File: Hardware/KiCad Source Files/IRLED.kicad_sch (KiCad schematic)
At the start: 14 parts

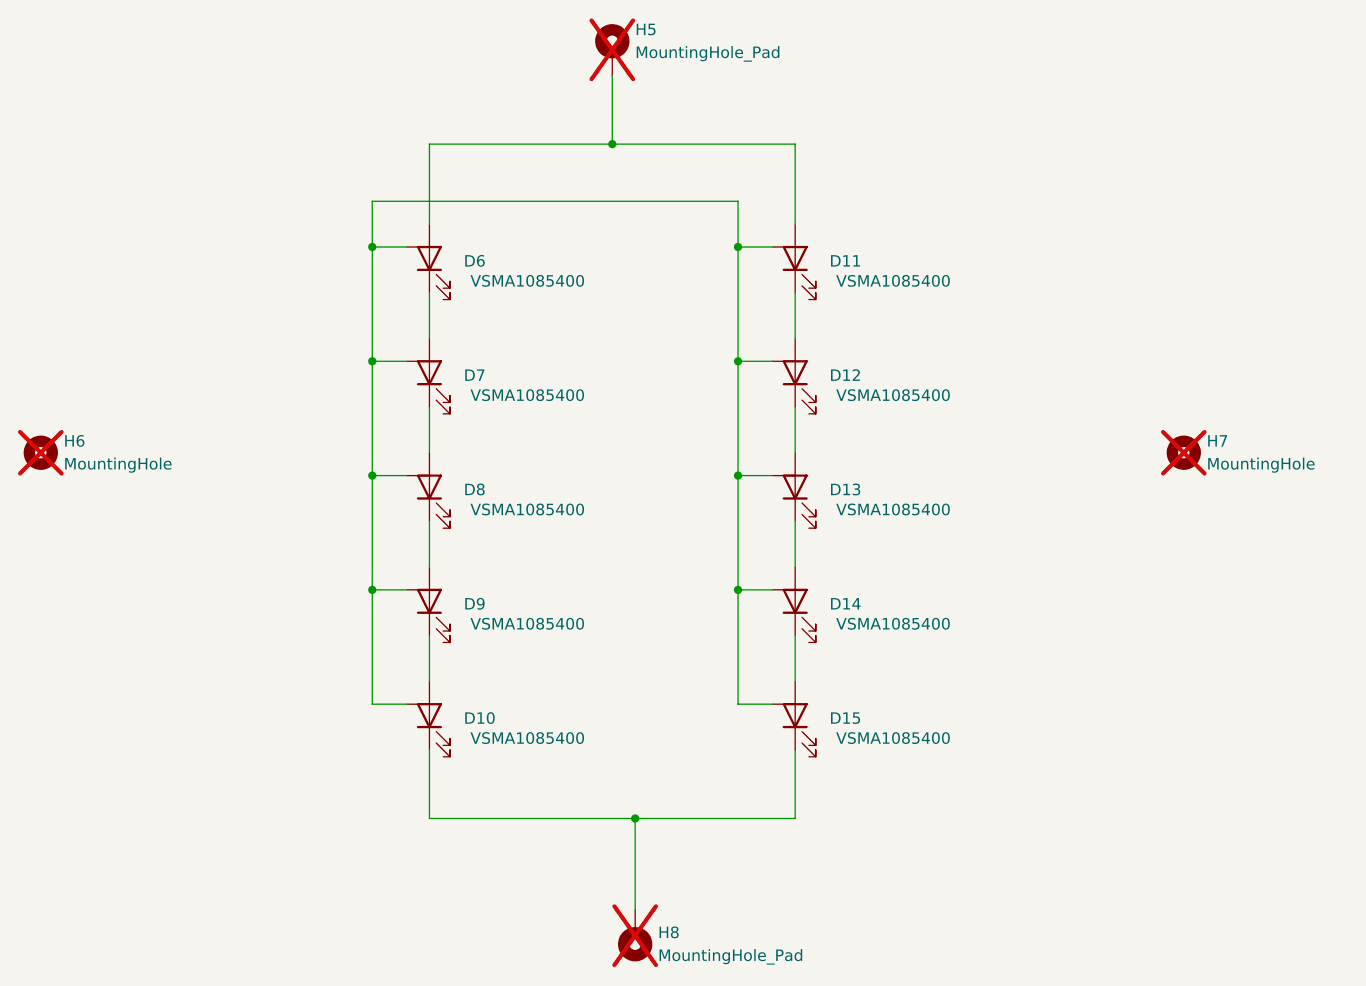
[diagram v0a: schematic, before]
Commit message: Replace IRLED1 [Original] with IRLED2. Fixes problem supporting cheap IRLED we found right before heading to fabrication.
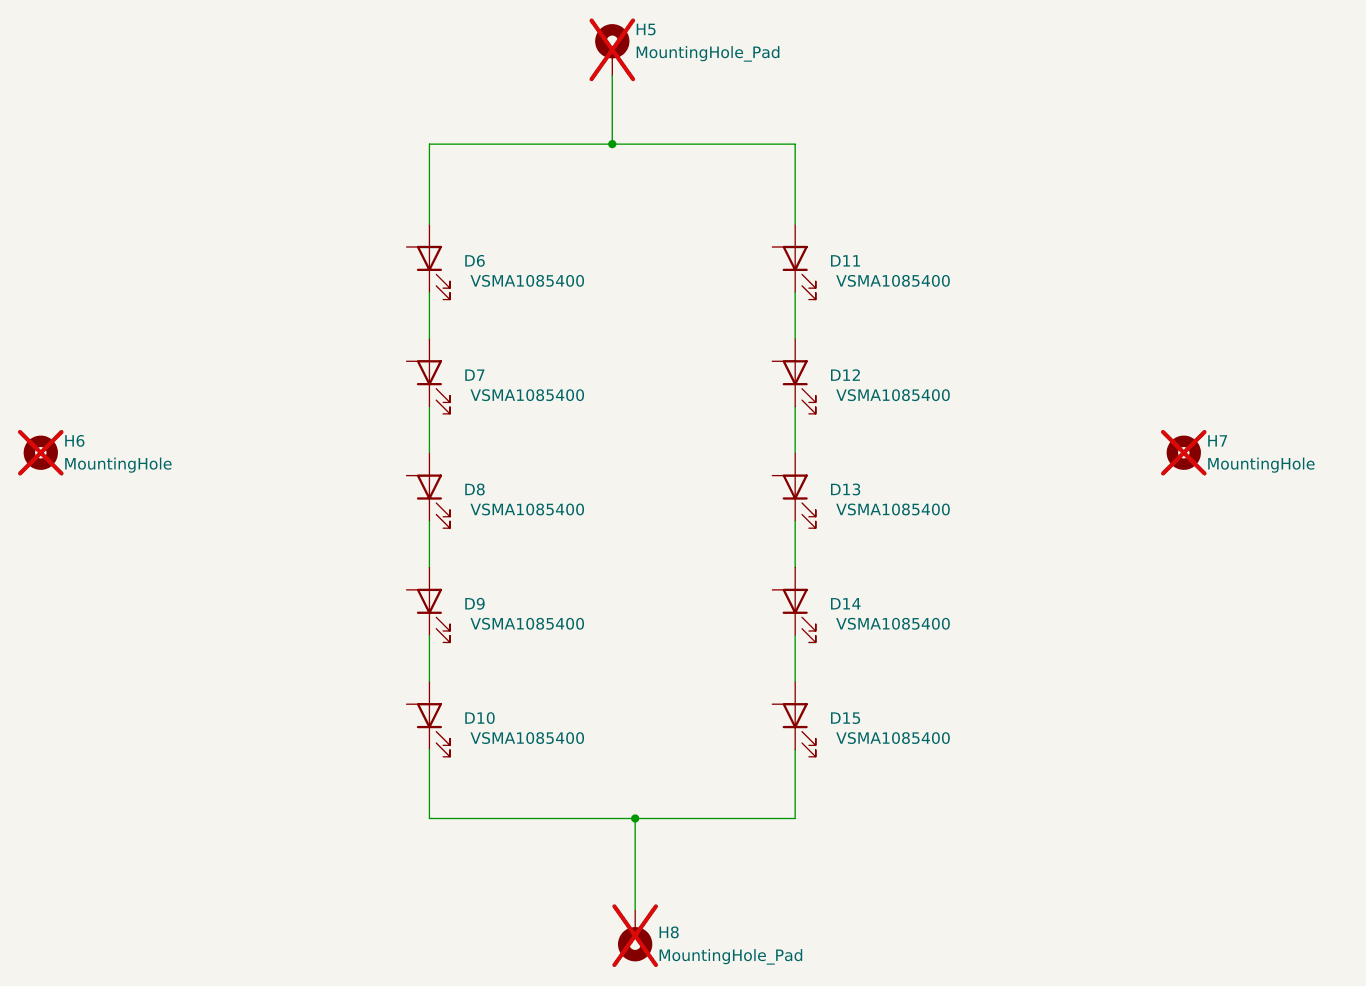
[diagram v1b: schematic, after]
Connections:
- now unconnected: D10.3 (P), D11.3 (P), D12.3 (P), D13.3 (P), D14.3 (P), D15.3 (P), D6.3 (P), D7.3 (P), D8.3 (P), D9.3 (P)
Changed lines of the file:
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@@
-	)
-	(junction
-		(at 109.22 93.98)
-		(diameter 0)
-		(color 0 0 0 0)
-	)
-	(junction
-		(at 109.22 68.58)
-		(diameter 0)
-		(color 0 0 0 0)
-	)
-	(junction
-		(at 149.86 81.28)
-		(diameter 0)
-		(color 0 0 0 0)
 	)
 	(junction
 		(at 135.89 57.15)
-		(diameter 0)
-		(color 0 0 0 0)
-	)
-	(junction
-		(at 149.86 93.98)
-		(diameter 0)
-		(color 0 0 0 0)
-	)
-	(junction
-		(at 149.86 68.58)
 		(diameter 0)
 		(color 0 0 0 0)
@@
 		(color 0 0 0 0)
 	)
-	(junction
-		(at 109.22 81.28)
-		(diameter 0)
-		(color 0 0 0 0)
-	)
-	(junction
-		(at 109.22 106.68)
-		(diameter 0)
-		(color 0 0 0 0)
-	)
-	(junction
-		(at 149.86 106.68)
-		(diameter 0)
-		(color 0 0 0 0)
-	)
 	(wire
 		(pts
-			(xy 149.86 93.98) (xy 149.86 81.28)
-		)
-		(stroke
-			(width 0)
-			(type default)
-		)
-	)
-	(wire
-		(pts
-			(xy 149.86 81.28) (xy 149.86 68.58)
-		)
-		(stroke
-			(width 0)
-			(type default)
-		)
-	)
-	(wire
-		(pts
-			(xy 149.86 81.28) (xy 153.67 81.28)
-		)
-		(stroke
-			(width 0)
-			(type default)
-		)
-	)
-	(wire
-		(pts
-			(xy 109.22 106.68) (xy 109.22 119.38)
+			(xy 156.21 86.36) (xy 156.21 91.44)
 		)
 		(stroke
@@
 	(wire
 		(pts
-			(xy 109.22 119.38) (xy 113.03 119.38)
-		)
-		(stroke
-			(width 0)
-			(type default)
-		)
-	)
-	(wire
-		(pts
-			(xy 149.86 106.68) (xy 149.86 93.98)
-		)
-		(stroke
-			(width 0)
-			(type default)
-		)
-	)
-	(wire
-		(pts
-			(xy 109.22 81.28) (xy 113.03 81.28)
+			(xy 115.57 86.36) (xy 115.57 91.44)
 		)
 		(stroke
@@
 	(wire
 		(pts
-			(xy 109.22 63.5) (xy 109.22 68.58)
-		)
-		(stroke
-			(width 0)
-			(type default)
-		)
-	)
-	(wire
-		(pts
 			(xy 115.57 132.08) (xy 138.43 132.08)
-		)
-		(stroke
-			(width 0)
-			(type default)
-		)
-	)
-	(wire
-		(pts
-			(xy 149.86 68.58) (xy 153.67 68.58)
-		)
-		(stroke
-			(width 0)
-			(type default)
-		)
-	)
-	(wire
-		(pts
-			(xy 156.21 86.36) (xy 156.21 91.44)
-		)
-		(stroke
-			(width 0)
-			(type default)
-		)
-	)
-	(wire
-		(pts
-			(xy 149.86 68.58) (xy 149.86 63.5)
-		)
-		(stroke
-			(width 0)
-			(type default)
-		)
-	)
-	(wire
-		(pts
-			(xy 109.22 93.98) (xy 113.03 93.98)
 		)
 		(stroke
@@
 	(wire
 		(pts
-			(xy 153.67 119.38) (xy 149.86 119.38)
-		)
-		(stroke
-			(width 0)
-			(type default)
-		)
-	)
-	(wire
-		(pts
 			(xy 156.21 73.66) (xy 156.21 78.74)
 		)
@@
 	(wire
 		(pts
-			(xy 109.22 68.58) (xy 109.22 81.28)
-		)
-		(stroke
-			(width 0)
-			(type default)
-		)
-	)
-	(wire
-		(pts
-			(xy 149.86 106.68) (xy 153.67 106.68)
-		)
-		(stroke
-			(width 0)
-			(type default)
-		)
-	)
-	(wire
-		(pts
-			(xy 109.22 81.28) (xy 109.22 93.98)
+			(xy 156.21 57.15) (xy 156.21 66.04)
 		)
 		(stroke
@@
 	(wire
 		(pts
-			(xy 149.86 119.38) (xy 149.86 106.68)
-		)
-		(stroke
-			(width 0)
-			(type default)
-		)
-	)
-	(wire
-		(pts
-			(xy 109.22 68.58) (xy 113.03 68.58)
-		)
-		(stroke
-			(width 0)
-			(type default)
-		)
-	)
-	(wire
-		(pts
 			(xy 156.21 132.08) (xy 156.21 124.46)
 		)
@@
 	(wire
 		(pts
-			(xy 149.86 63.5) (xy 109.22 63.5)
-		)
-		(stroke
-			(width 0)
-			(type default)
-		)
-	)
-	(wire
-		(pts
 			(xy 115.57 99.06) (xy 115.57 104.14)
-		)
-		(stroke
-			(width 0)
-			(type default)
-		)
-	)
-	(wire
-		(pts
-			(xy 109.22 106.68) (xy 113.03 106.68)
-		)
-		(stroke
-			(width 0)
-			(type default)
-		)
-	)
-	(wire
-		(pts
-			(xy 115.57 57.15) (xy 115.57 66.04)
-		)
-		(stroke
-			(width 0)
-			(type default)
-		)
-	)
-	(wire
-		(pts
-			(xy 109.22 93.98) (xy 109.22 106.68)
-		)
-		(stroke
-			(width 0)
-			(type default)
-		)
-	)
-	(wire
-		(pts
-			(xy 156.21 57.15) (xy 156.21 66.04)
 		)
 		(stroke
@@
 	(wire
 		(pts
-			(xy 149.86 93.98) (xy 153.67 93.98)
+			(xy 115.57 57.15) (xy 115.57 66.04)
 		)
 		(stroke
-			(width 0)
-			(type default)
-		)
-	)
-	(wire
-		(pts
-			(xy 115.57 86.36) (xy 115.57 91.44)
-		)
-		(stroke
